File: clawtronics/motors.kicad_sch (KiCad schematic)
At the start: 37 parts, among them J1 Screw_Terminal_01x06, U1 DRV8876PWPR, U5 DRV8876PWPR, U6 DRV8876PWPR

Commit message: pcb progress
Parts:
- removed U1, U6: DRV8876PWPR, DRV8876PWPR:IC_DRV8876PWPR, symbol Driver_Motor:DRV8876PWPR
- added U3, U4: DRV8876PWPR, Motors:moto, symbol Driver_Motor:DRV8876PWPR
- U5: footprint DRV8876PWPR:IC_DRV8876PWPR -> Motors:moto
- renumbered C7 to C10, C17 to C11, C8 to C12, C6 to C13, C2 to C14, C9 to C15, C10 to C16, C3 to C17, C11 to C18, C4 to C19, C18 to C20, C5 to C21, C12 to C22, C1 to C23, C13 to C6, C14 to C7, C15 to C8, C16 to C9, J1 to J5, R15 to R10, R7 to R11, R8 to R12, R9 to R13, R3 to R14, R2 to R15, R10 to R16, R5 to R17, R4 to R18, R16 to R19, R11 to R20, R1 to R21, R12 to R7, R13 to R8, R14 to R9
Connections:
- net +24V: now also U3.11 (VM), U4.11 (VM)
- net +3.3V: no longer R11.1, R14.1, R19.1, R20.1, R21.1, R7.1
- net GND: now also U3.15 (GND), U3.16 (PMODE), U3.17 (EXP), U3.7 (IMODE), U3.9 (PGND), U4.15 (GND), U4.16 (PMODE), U4.17 (EXP), U4.7 (IMODE), U4.9 (PGND)
- net GPIO1: now also U3.1 (EN/IN1)
- net GPIO10: now also U5.2 (PH/IN2)
- net GPIO2: now also U3.2 (PH/IN2)
- net GPIO21: now also U3.4 (~{NFAULT}), U4.4 (~{NFAULT})
- net GPIO7: now also U4.1 (EN/IN1); no longer U5.1 (EN/IN1)
- net GPIO8: now also U4.2 (PH/IN2); no longer U5.2 (PH/IN2)
- net GPIO9: now also U5.1 (EN/IN1)
- net at J5.6 (Pin_6): now also U5.10 (OUT2)
- net at C8.1: now also U5.12 (VCP)
- net at C20.1: now also U5.13 (CPH)
- net at C20.2: now also U5.14 (CPL)
- net at C7.2, R7.2, R8.1: now also U5.5 (VREF)
- net at R10.1, R9.2: now also U5.6 (IPROPI)
- net at J5.5 (Pin_5): now also U5.8 (OUT1)
- net at R13.2, R16.1: now also U4.6 (IPROPI); no longer U5.6 (IPROPI)
- net at C14.2, R14.2, R15.1: now also U3.5 (VREF)
- net at J5.2 (Pin_2): now also U3.10 (OUT2)
- net at C17.1: now also U3.12 (VCP)
- net at C23.1: now also U3.13 (CPH)
- net at C23.2: now also U3.14 (CPL)
- net at R17.2, R18.1: now also U3.6 (IPROPI)
- net at J5.1 (Pin_1): now also U3.8 (OUT1)
- net at C22.1: now also U4.13 (CPH); no longer U5.13 (CPH)
- net at C22.2: now also U4.14 (CPL); no longer U5.14 (CPL)
- net at C12.2, R11.2, R12.1: now also U4.5 (VREF); no longer U5.5 (VREF)
- net at C15.1: now also U4.12 (VCP); no longer U5.12 (VCP)
- net at J5.4 (Pin_4): now also U4.10 (OUT2); no longer U5.10 (OUT2)
- net at J5.3 (Pin_3): now also U4.8 (OUT1); no longer U5.8 (OUT1)
- new net +3V3: R11.1, R14.1, R19.1, R20.1, R21.1, R7.1, U3.3 (NSLEEP), U4.3 (NSLEEP)

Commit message: add pcb
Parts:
- renumbered U5 to U3, U3 to U5
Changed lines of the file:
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@@
 		(dnp no)
 		(fields_autoplaced yes)
-		(property "Reference" "U3"
+		(property "Reference" "U5"
 			(at 157.48 17.78 0)
 			(show_name no)
@@
 			(project "clawtronics"
 				(path "/cc1ca336-3c31-444e-9aa4-ec0173cb8745"
-					(reference "U3")
+					(reference "U5")
 					(unit 1)
 				)
@@
 		(dnp no)
 		(fields_autoplaced yes)
-		(property "Reference" "U5"
+		(property "Reference" "U3"
 			(at 99.06 132.08 0)
 			(show_name no)
@@
 			(project "clawtronics"
 				(path "/cc1ca336-3c31-444e-9aa4-ec0173cb8745"
-					(reference "U5")
-					(unit 1)
-				)
+					(reference "U3")
+					(unit 1)
+				)

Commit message: figured out switches
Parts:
- J5: footprint Connector_Phoenix_MSTB:PhoenixContact_MSTBV_2,5_6-GF-5,08_1x06_P5.08mm_Vertical_ThreadedFlange_MountHole -> TerminalBlock_MetzConnect:TerminalBlock_MetzConnect_Type011_RT05506HBLC_1x06_P5.00mm_Horizontal

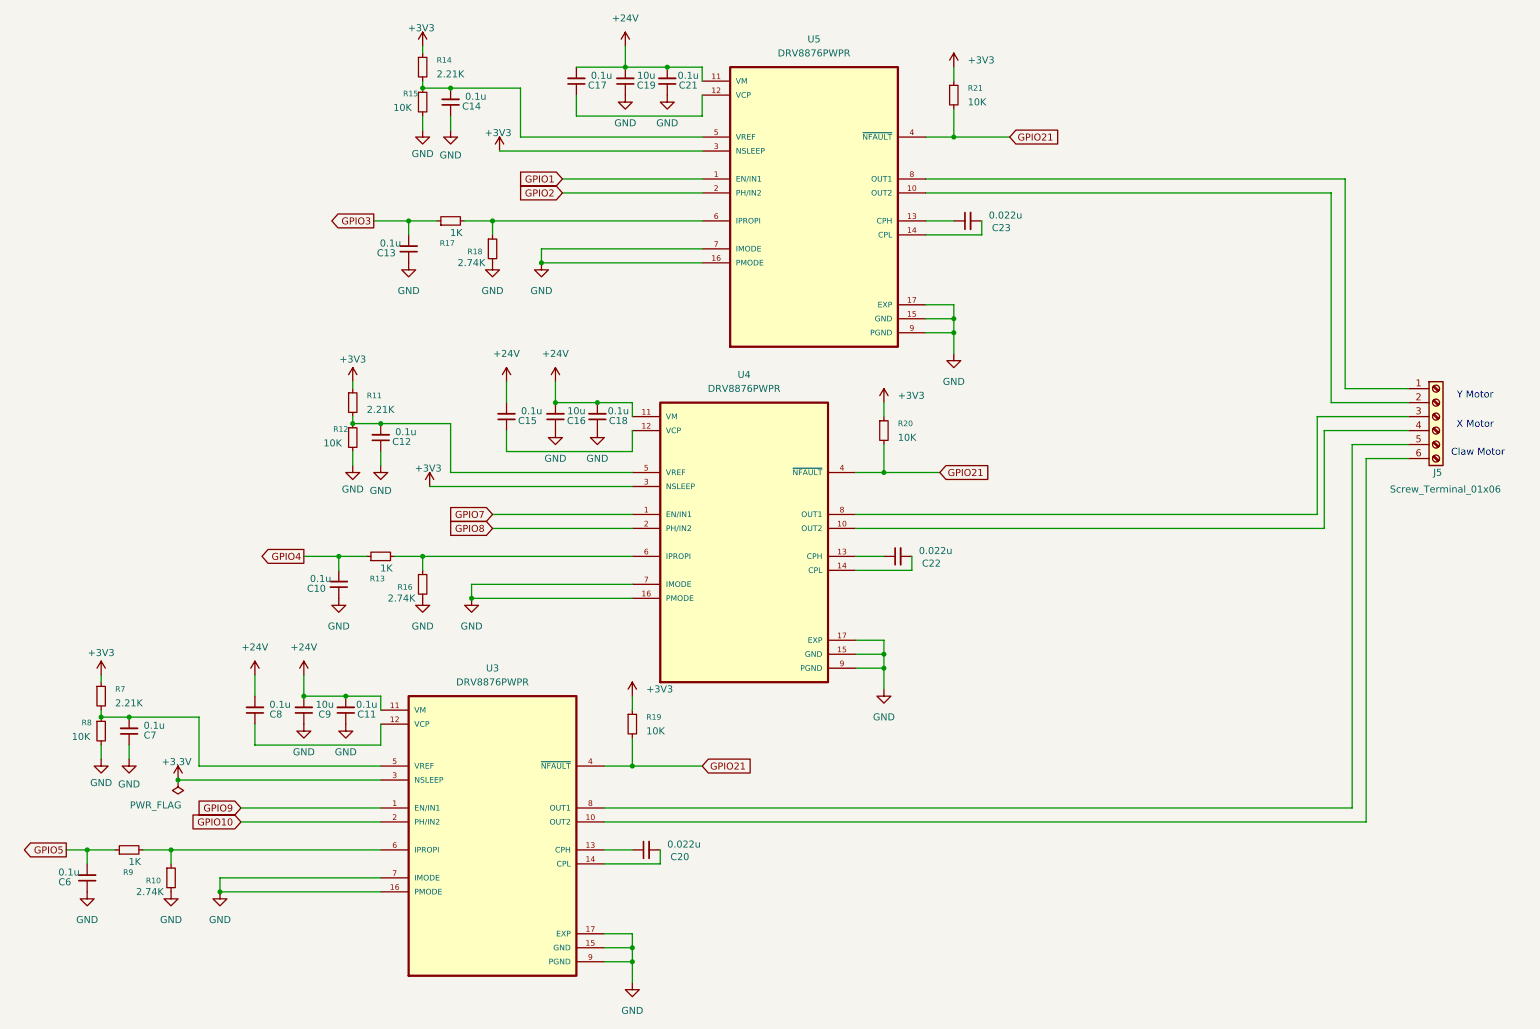
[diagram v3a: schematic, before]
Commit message: layout with hierarchical sheets
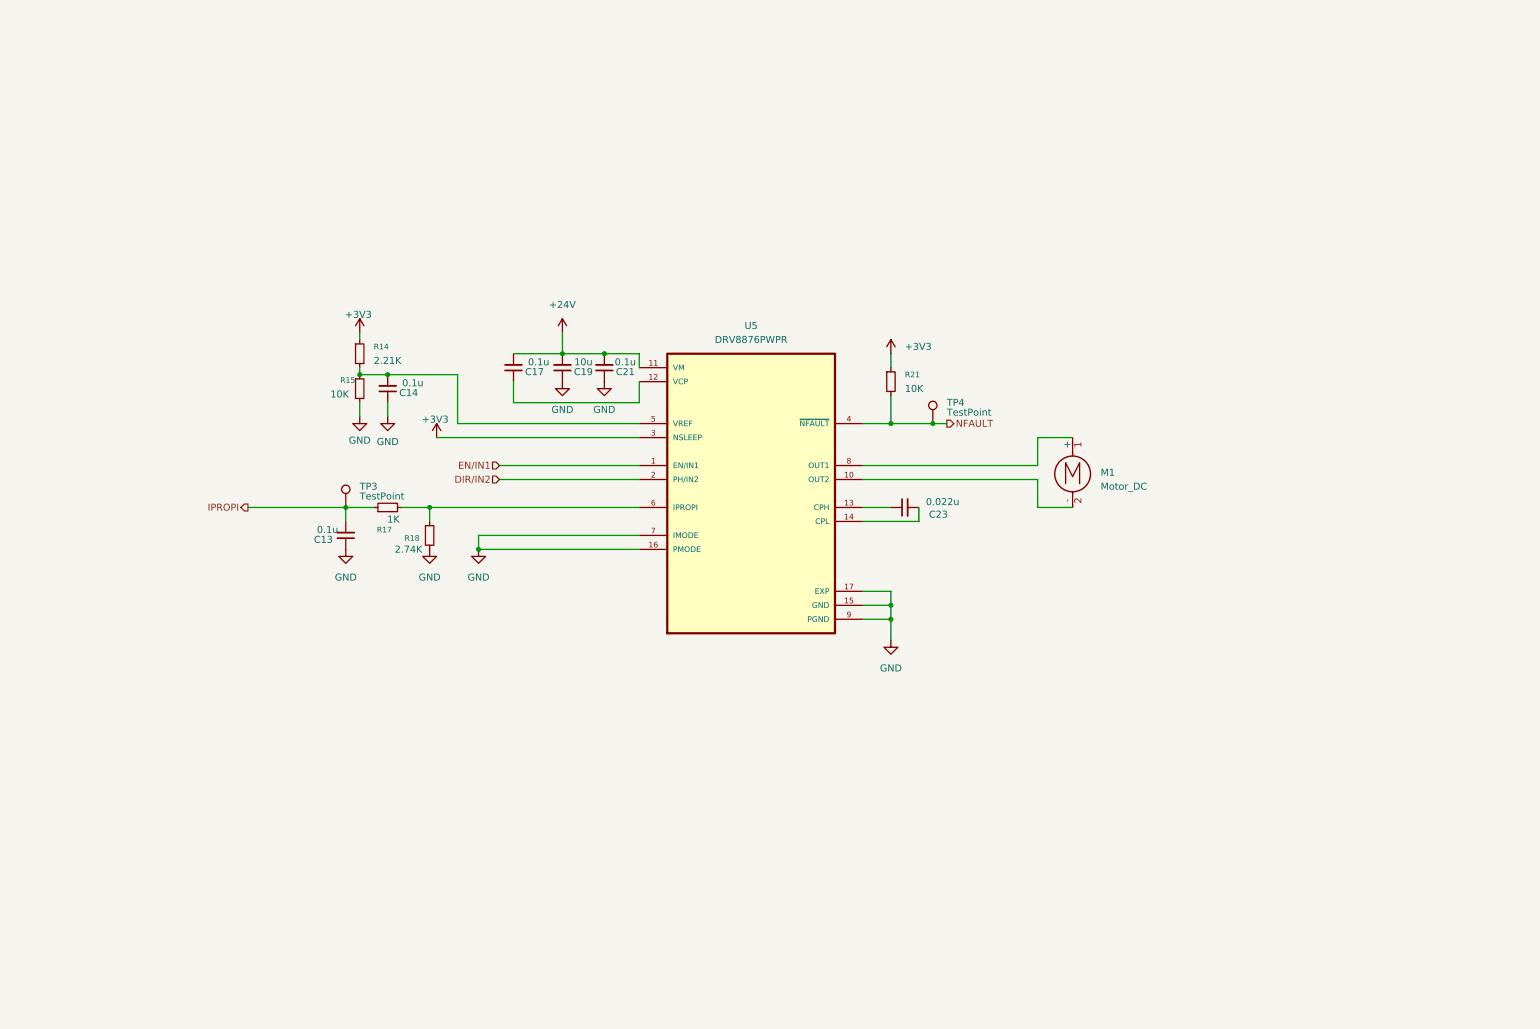
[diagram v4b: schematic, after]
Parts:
- removed C10, C11, C12, C15, C18, C6, C7, C8: 0.1u, Capacitor_SMD:C_0603_1608Metric, symbol Device:C_Small
- removed C16, C9: 10u, Capacitor_SMD:C_0603_1608Metric, symbol Device:C_Small
- removed C20, C22: 0.022u, Capacitor_SMD:C_0603_1608Metric, symbol Device:C_Small
- removed J5: Screw_Terminal_01x06, TerminalBlock_MetzConnect:TerminalBlock_MetzConnect_Type011_RT05506HBLC_1x06_P5.00mm_Horizontal, symbol Connector:Screw_Terminal_01x06
- removed R10, R16: 2.74K, Resistor_SMD:R_0603_1608Metric, symbol Device:R_Small
- removed R11, R7: 2.21K, Resistor_SMD:R_0603_1608Metric, symbol Device:R_Small
- removed R12, R19, R20, R8: 10K, Resistor_SMD:R_0603_1608Metric, symbol Device:R_Small
- removed R13, R9: 1K, Resistor_SMD:R_0603_1608Metric, symbol Device:R_Small
- removed U3, U4: DRV8876PWPR, Motors:moto, symbol Driver_Motor:DRV8876PWPR
- added M1: Motor_DC, TerminalBlock_Phoenix:TerminalBlock_Phoenix_MKDS-1,5-2_1x02_P5.00mm_Horizontal, symbol Motor:Motor_DC
- added TP3, TP4: TestPoint, TestPoint:TestPoint_Pad_1.0x1.0mm, symbol Connector:TestPoint
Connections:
- net at U5.10 (OUT2): now also M1.2 (-)
- net at U5.8 (OUT1): now also M1.1 (+)
- net GPIO1 renamed EN/IN1
- net GPIO2 renamed DIR/IN2
- net GPIO21 renamed NFAULT
- net NFAULT: now also TP4.1
- net GPIO3 renamed IPROPI
- net IPROPI: now also TP3.1
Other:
- note removed: "Claw Motor"
- note removed: "X Motor"
- note removed: "Y Motor"
- moved on the sheet: C13, C14, C17, C19, C21, C23, R14, R15, R17, R18, R21, U5

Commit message: update BOM with PNs
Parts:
- C13, C14, C17, C21: Part Number (none) -> 0603B104K101XD
- C19: Part Number (none) -> 0603W106M6R3XD
- C23: Part Number (none) -> 0603B223K500SD
- M1: Part Number (none) -> 1729128
- R14: Part Number (none) -> RMCF0603FT2K21
- R15, R21: Part Number (none) -> RC0603FR-0710KL
- R17: Part Number (none) -> RMCF0603FT1K00
- R18: Part Number (none) -> RMCF0603FT2K74
- TP3, TP4: now not fitted
- U5: Part Number (none) -> DRV8876PWPR
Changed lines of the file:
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@@
 		(on_board yes)
 		(in_pos_files yes)
-		(dnp no)
+		(dnp yes)
 		(property "Reference" "TP3"
 			(at 74.93 99.06 0)
@@
 		)
 		(property "Description" "test point"
+			(at 72.39 102.87 0)
+			(hide yes)
+			(show_name no)
+			(do_not_autoplace no)
+			(effects
+				(font
+					(size 1.27 1.27)
+				)
+			)
+		)
+		(property "Part Number" ""
 			(at 72.39 102.87 0)
 			(hide yes)
@@
 			)
 		)
-		(property "Datasheet" ""
+		(property "Datasheet" "https://mm.digikey.com/Volume0/opasdata/d220001/medias/docus/6482/3372_0603B104K101XD.pdf"
 			(at 80.01 81.28 0)
 			(hide yes)
@@
 		)
 		(property "Description" "Unpolarized capacitor, small symbol"
+			(at 80.01 81.28 0)
+			(hide yes)
+			(show_name no)
+			(do_not_autoplace no)
+			(effects
+				(font
+					(size 1.27 1.27)
+				)
+			)
+		)
+		(property "Part Number" "0603B104K101XD"
 			(at 80.01 81.28 0)
 			(hide yes)
@@
 			)
 		)
-		(property "Datasheet" ""
+		(property "Datasheet" "https://mm.digikey.com/Volume0/opasdata/d220001/medias/docus/6490/3372_0603B223K500SD.pdf"
 			(at 173.99 102.87 0)
 			(hide yes)
@@
 		(property "Description" "Unpolarized capacitor, small symbol"
 			(at 173.99 102.87 0)
+			(hide yes)
+			(show_name no)
+			(do_not_autoplace no)
+			(effects
+				(font
+					(size 1.27 1.27)
+				)
+			)
+		)
+		(property "Part Number" "0603B223K500SD"
+			(at 173.99 102.87 90)
 			(hide yes)
 			(show_name no)
@@
 			)
 		)
+		(property "Part Number" "RC0603FR-0710KL"
+			(at 171.45 80.01 0)
+			(hide yes)
+			(show_name no)
+			(do_not_autoplace no)
+			(effects
+				(font
+					(size 1.27 1.27)
+				)
+			)
+		)
 		(pin "2"
 		)
@@
 		)
 		(property "Description" "Resistor, small symbol"
+			(at 74.93 81.28 0)
+			(hide yes)
+			(show_name no)
+			(do_not_autoplace no)
+			(effects
+				(font
+					(size 1.27 1.27)
+				)
+			)
+		)
+		(property "Part Number" "RC0603FR-0710KL"
 			(at 74.93 81.28 0)
 			(hide yes)
@@
 			)
 		)
+		(property "Part Number" "RMCF0603FT2K21"
+			(at 74.93 74.93 0)
+			(hide yes)
+			(show_name no)
+			(do_not_autoplace no)
+			(effects
+				(font
+					(size 1.27 1.27)
+				)
+			)
+		)
 		(pin "2"
 		)
@@
 			)
 		)
-		(property "Datasheet" ""
+		(property "Datasheet" "https://mm.digikey.com/Volume0/opasdata/d220001/medias/docus/6482/3372_0603W106M6R3XD.pdf"
 			(at 111.76 77.47 0)
 			(hide yes)
@@
 		)
 		(property "Description" "Unpolarized capacitor, small symbol"
+			(at 111.76 77.47 0)
+			(hide yes)
+			(show_name no)
+			(do_not_autoplace no)
+			(effects
+				(font
+					(size 1.27 1.27)
+				)
+			)
+		)
+		(property "Part Number" "0603W106M6R3XD"
 			(at 111.76 77.47 0)
 			(hide yes)
@@
 			)
 		)
+		(property "Part Number" "DRV8876PWPR"
+			(at 146.05 100.33 0)
+			(hide yes)
+			(show_name no)
+			(do_not_autoplace no)
+			(effects
+				(font
+					(size 1.27 1.27)
+				)
+			)
+		)
 		(pin "14"
 		)
@@
 			)
 		)
+		(property "Part Number" "RMCF0603FT2K74"
+			(at 87.63 107.95 0)
+			(hide yes)
+			(show_name no)
+			(do_not_autoplace no)
+			(effects
+				(font
+					(size 1.27 1.27)
+				)
+			)
+		)
 		(pin "2"
 		)
@@
 		(on_board yes)
 		(in_pos_files yes)
-		(dnp no)
+		(dnp yes)
 		(property "Reference" "TP4"
 			(at 181.61 83.82 0)
@@
 		)
 		(property "Description" "test point"
+			(at 179.07 87.63 0)
+			(hide yes)
+			(show_name no)
+			(do_not_autoplace no)
+			(effects
+				(font
+					(size 1.27 1.27)
+				)
+			)
+		)
+		(property "Part Number" ""
 			(at 179.07 87.63 0)
 			(hide yes)
@@
 			)
 		)
+		(property "Part Number" "1729128"
+			(at 204.47 95.25 0)
+			(hide yes)
+			(show_name no)
+			(do_not_autoplace no)
+			(effects
+				(font
+					(size 1.27 1.27)
+				)
+			)
+		)
 		(pin "1"
 		)
@@
 			)
 		)
-		(property "Datasheet" ""
+		(property "Datasheet" "https://mm.digikey.com/Volume0/opasdata/d220001/medias/docus/6482/3372_0603B104K101XD.pdf"
 			(at 72.39 107.95 0)
 			(hide yes)
@@
 		)
 		(property "Description" "Unpolarized capacitor, small symbol"
+			(at 72.39 107.95 0)
+			(hide yes)
+			(show_name no)
+			(do_not_autoplace no)
+			(effects
+				(font
+					(size 1.27 1.27)
+				)
+			)
+		)
+		(property "Part Number" "0603B104K101XD"
 			(at 72.39 107.95 0)
 			(hide yes)
@@
 			)
 		)
-		(property "Datasheet" ""
+		(property "Datasheet" "https://mm.digikey.com/Volume0/opasdata/d220001/medias/docus/6482/3372_0603B104K101XD.pdf"
 			(at 119.38 77.47 0)
 			(hide yes)
@@
 		)
 		(property "Description" "Unpolarized capacitor, small symbol"
+			(at 119.38 77.47 0)
+			(hide yes)
+			(show_name no)
+			(do_not_autoplace no)
+			(effects
+				(font
+					(size 1.27 1.27)
+				)
+			)
+		)
+		(property "Part Number" "0603B104K101XD"
 			(at 119.38 77.47 0)
 			(hide yes)
@@
 			)
 		)
+		(property "Part Number" "RMCF0603FT1K00"
+			(at 80.01 102.87 90)
+			(hide yes)
+			(show_name no)
+			(do_not_autoplace no)
+			(effects
+				(font
+					(size 1.27 1.27)
+				)
+			)
+		)
 		(pin "2"
 		)
@@
 			)
 		)
-		(property "Datasheet" ""
+		(property "Datasheet" "https://mm.digikey.com/Volume0/opasdata/d220001/medias/docus/6482/3372_0603B104K101XD.pdf"
 			(at 102.87 77.47 0)
 			(hide yes)
@@
 			(at 102.87 77.47 0)
 			(hide yes)
+			(show_name no)
+			(do_not_autoplace no)
+			(effects
+				(font
+					(size 1.27 1.27)
+				)
+			)
+		)
+		(property "Part Number" "0603B104K101XD"
+			(at 102.87 77.47 0)
+			(hide yes)

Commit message: update footprints
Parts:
- C13, C14, C17, C21: Part Number 0603B104K101XD -> C0603C104J3RACTU
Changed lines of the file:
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@@
 			)
 		)
-		(property "Datasheet" "https://mm.digikey.com/Volume0/opasdata/d220001/medias/docus/6482/3372_0603B104K101XD.pdf"
+		(property "Datasheet" "https://yageogroup.com/content/datasheet/asset/file/KEM_C1002_X7R_SMD"
 			(at 80.01 81.28 0)
 			(hide yes)
@@
 			)
 		)
-		(property "Part Number" "0603B104K101XD"
+		(property "Part Number" "C0603C104J3RACTU"
 			(at 80.01 81.28 0)
 			(hide yes)
@@
 			)
 		)
-		(property "Datasheet" "https://mm.digikey.com/Volume0/opasdata/d220001/medias/docus/6482/3372_0603B104K101XD.pdf"
+		(property "Datasheet" "https://yageogroup.com/content/datasheet/asset/file/KEM_C1002_X7R_SMD"
 			(at 72.39 107.95 0)
 			(hide yes)
@@
 			)
 		)
-		(property "Part Number" "0603B104K101XD"
+		(property "Part Number" "C0603C104J3RACTU"
 			(at 72.39 107.95 0)
 			(hide yes)
@@
 			)
 		)
-		(property "Datasheet" "https://mm.digikey.com/Volume0/opasdata/d220001/medias/docus/6482/3372_0603B104K101XD.pdf"
+		(property "Datasheet" "https://yageogroup.com/content/datasheet/asset/file/KEM_C1002_X7R_SMD"
 			(at 119.38 77.47 0)
 			(hide yes)
@@
 			)
 		)
-		(property "Part Number" "0603B104K101XD"
+		(property "Part Number" "C0603C104J3RACTU"
 			(at 119.38 77.47 0)
 			(hide yes)
@@
 			)
 		)
-		(property "Datasheet" "https://mm.digikey.com/Volume0/opasdata/d220001/medias/docus/6482/3372_0603B104K101XD.pdf"
+		(property "Datasheet" "https://yageogroup.com/content/datasheet/asset/file/KEM_C1002_X7R_SMD"
 			(at 102.87 77.47 0)
 			(hide yes)
@@
 			)
 		)
-		(property "Part Number" "0603B104K101XD"
+		(property "Part Number" "C0603C104J3RACTU"
 			(at 102.87 77.47 0)
 			(hide yes)
